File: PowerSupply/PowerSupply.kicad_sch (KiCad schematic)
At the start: 8 parts, among them J1 POWER, J2 CONTROL, J3 LASER, U0 AL8861Y-13

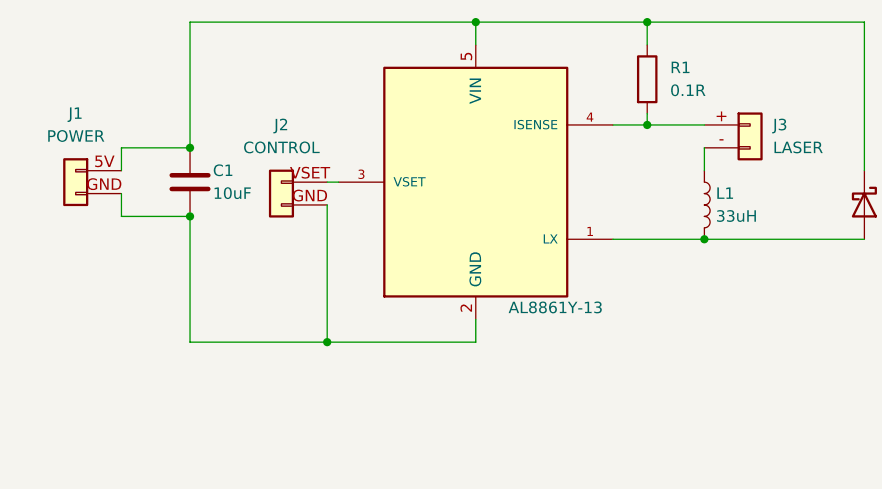
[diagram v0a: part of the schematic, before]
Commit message: update powersupply
edit resistor R1 (controling current) value, add pulldown on VSET, add descriptions
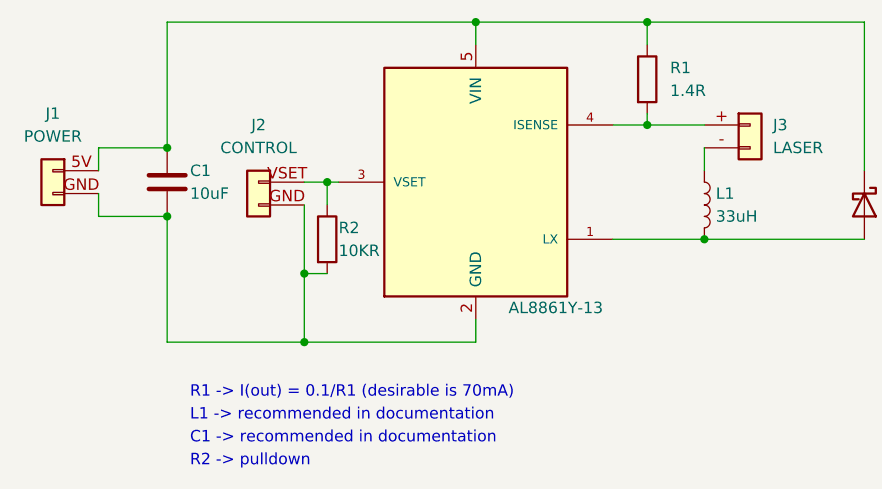
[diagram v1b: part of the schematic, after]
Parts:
- added R2: 10KR, symbol Device:R
- R1: value 0.1R -> 1.4R
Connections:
- net at C1.2, J1.GND, J2.GND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: now also R2.2
- net at J2.VSET, U0.3 (VSET): now also R2.1
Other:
- note added: "C1 -> recommended in documentation"
- note added: "L1 -> recommended in documentation"
- note added: "R1 -> I(out) = 0.1/R1 (desirable is 70mA)"
- note added: "R2 -> pulldown"
- moved on the sheet: C1, J1, J2
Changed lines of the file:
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@@
 (kicad_sch (version 20211123) (generator eeschema)
   (paper "A4")
-  (junction (at 110.49 90.17) (diameter 0) (color 0 0 0 0)
+  (junction (at 107.95 90.17) (diameter 0) (color 0 0 0 0)
   )
   (junction (at 161.29 76.2) (diameter 0) (color 0 0 0 0)
   )
-  (junction (at 125.73 111.76) (diameter 0) (color 0 0 0 0)
-  )
-  (junction (at 110.49 97.79) (diameter 0) (color 0 0 0 0)
+  (junction (at 107.95 97.79) (diameter 0) (color 0 0 0 0)
   )
   (junction (at 142.24 76.2) (diameter 0) (color 0 0 0 0)
   )
+  (junction (at 125.73 93.98) (diameter 0) (color 0 0 0 0)
+  )
   (junction (at 167.64 100.33) (diameter 0) (color 0 0 0 0)
   )
+  (junction (at 123.19 104.14) (diameter 0) (color 0 0 0 0)
+  )
+  (junction (at 123.19 111.76) (diameter 0) (color 0 0 0 0)
+  )
   (junction (at 161.29 87.63) (diameter 0) (color 0 0 0 0)
   )
-  (wire (pts (xy 102.87 92.71) (xy 102.87 90.17))
+  (wire (pts (xy 100.33 92.71) (xy 100.33 90.17))
     (stroke (width 0) (type default) (color 0 0 0 0))
   )
@@
     (stroke (width 0) (type default) (color 0 0 0 0))
   )
-  (wire (pts (xy 102.87 90.17) (xy 110.49 90.17))
-    (stroke (width 0) (type default) (color 0 0 0 0))
-  )
-  (wire (pts (xy 110.49 76.2) (xy 142.24 76.2))
+  (wire (pts (xy 123.19 104.14) (xy 125.73 104.14))
+    (stroke (width 0) (type default) (color 0 0 0 0))
+  )
+  (wire (pts (xy 100.33 90.17) (xy 107.95 90.17))
+    (stroke (width 0) (type default) (color 0 0 0 0))
+  )
+  (wire (pts (xy 107.95 76.2) (xy 142.24 76.2))
     (stroke (width 0) (type default) (color 0 0 0 0))
   )
@@
     (stroke (width 0) (type default) (color 0 0 0 0))
   )
-  (wire (pts (xy 110.49 97.79) (xy 110.49 111.76))
+  (wire (pts (xy 107.95 97.79) (xy 107.95 111.76))
     (stroke (width 0) (type default) (color 0 0 0 0))
   )
@@
     (stroke (width 0) (type default) (color 0 0 0 0))
   )
+  (wire (pts (xy 125.73 93.98) (xy 127 93.98))
+    (stroke (width 0) (type default) (color 0 0 0 0))
+  )
   (wire (pts (xy 185.42 76.2) (xy 161.29 76.2))
     (stroke (width 0) (type default) (color 0 0 0 0))
   )
-  (wire (pts (xy 125.73 111.76) (xy 142.24 111.76))
-    (stroke (width 0) (type default) (color 0 0 0 0))
-  )
   (wire (pts (xy 142.24 111.76) (xy 142.24 109.22))
     (stroke (width 0) (type default) (color 0 0 0 0))
   )
+  (wire (pts (xy 123.19 111.76) (xy 142.24 111.76))
+    (stroke (width 0) (type default) (color 0 0 0 0))
+  )
   (wire (pts (xy 142.24 76.2) (xy 161.29 76.2))
     (stroke (width 0) (type default) (color 0 0 0 0))
@@
     (stroke (width 0) (type default) (color 0 0 0 0))
   )
-  (wire (pts (xy 125.73 96.52) (xy 125.73 111.76))
-    (stroke (width 0) (type default) (color 0 0 0 0))
-  )
-  (wire (pts (xy 125.73 93.98) (xy 127 93.98))
-    (stroke (width 0) (type default) (color 0 0 0 0))
-  )
-  (wire (pts (xy 110.49 90.17) (xy 110.49 76.2))
-    (stroke (width 0) (type default) (color 0 0 0 0))
-  )
-  (wire (pts (xy 102.87 95.25) (xy 102.87 97.79))
+  (wire (pts (xy 123.19 96.52) (xy 123.19 104.14))
+    (stroke (width 0) (type default) (color 0 0 0 0))
+  )
+  (wire (pts (xy 123.19 104.14) (xy 123.19 111.76))
+    (stroke (width 0) (type default) (color 0 0 0 0))
+  )
+  (wire (pts (xy 123.19 93.98) (xy 125.73 93.98))
+    (stroke (width 0) (type default) (color 0 0 0 0))
+  )
+  (wire (pts (xy 107.95 90.17) (xy 107.95 76.2))
+    (stroke (width 0) (type default) (color 0 0 0 0))
+  )
+  (wire (pts (xy 125.73 93.98) (xy 125.73 96.52))
+    (stroke (width 0) (type default) (color 0 0 0 0))
+  )
+  (wire (pts (xy 100.33 95.25) (xy 100.33 97.79))
     (stroke (width 0) (type default) (color 0 0 0 0))
   )
@@
     (stroke (width 0) (type default) (color 0 0 0 0))
   )
-  (wire (pts (xy 110.49 111.76) (xy 125.73 111.76))
-    (stroke (width 0) (type default) (color 0 0 0 0))
-  )
-  (wire (pts (xy 102.87 97.79) (xy 110.49 97.79))
-    (stroke (width 0) (type default) (color 0 0 0 0))
+  (wire (pts (xy 107.95 111.76) (xy 123.19 111.76))
+    (stroke (width 0) (type default) (color 0 0 0 0))
+  )
+  (wire (pts (xy 100.33 97.79) (xy 107.95 97.79))
+    (stroke (width 0) (type default) (color 0 0 0 0))
+  )
+  (text "C1 -> recommended in documentation" (at 110.49 123.19 0)
+    (effects (font (size 1.27 1.27)) (justify left bottom))
+  )
+  (text "R2 -> pulldown" (at 110.49 125.73 0)
+    (effects (font (size 1.27 1.27)) (justify left bottom))
+  )
+  (text "R1 -> I(out) = 0.1/R1 (desirable is 70mA)" (at 110.49 118.11 0)
+    (effects (font (size 1.27 1.27)) (justify left bottom))
+  )
+  (text "L1 -> recommended in documentation\n" (at 110.49 120.65 0)
+    (effects (font (size 1.27 1.27)) (justify left bottom))
   )
   (symbol (lib_id "Connector_Generic:Conn_01x02") (at 172.72 87.63 0) (unit 1)
@@
       (effects (font (size 1.27 1.27)) (justify left))
     )
-    (property "Value" "0.1R" (id 1) (at 163.83 83.8199 0)
+    (property "Value" "1.4R" (id 1) (at 163.83 83.8199 0)
       (effects (font (size 1.27 1.27)) (justify left))
     )
@@
     (pin "5")
   )
+  (symbol (lib_id "Device:R") (at 125.73 100.33 0) (unit 1)
+    (in_bom yes) (on_board yes)
+    (property "Reference" "R2" (id 0) (at 127 99.06 0)
+      (effects (font (size 1.27 1.27)) (justify left))
+    )
+    (property "Value" "10KR" (id 1) (at 127 101.6 0)
+      (effects (font (size 1.27 1.27)) (justify left))
+    )
+    (property "Footprint" "" (id 2) (at 123.952 100.33 90)
+      (effects (font (size 1.27 1.27)) hide)
+    )
+    (property "Datasheet" "~" (id 3) (at 125.73 100.33 0)
+      (effects (font (size 1.27 1.27)) hide)
+    )
+    (pin "1")
+    (pin "2")
+  )
   (symbol (lib_id "Device:L") (at 167.64 96.52 0) (unit 1)
     (in_bom yes) (on_board yes) (fields_autoplaced)
@@
     (pin "2")
   )
-  (symbol (lib_name "Conn_01x02_1") (lib_id "Connector_Generic:Conn_01x02") (at 97.79 92.71 0) (mirror y) (unit 1)
-    (in_bom yes) (on_board yes) (fields_autoplaced)
-    (property "Reference" "J1" (id 0) (at 97.79 86.36 0))
-    (property "Value" "POWER" (id 1) (at 97.79 88.9 0))
-    (property "Footprint" "" (id 2) (at 97.79 92.71 0)
-      (effects (font (size 1.27 1.27)) hide)
-    )
-    (property "Datasheet" "~" (id 3) (at 97.79 92.71 0)
+  (symbol (lib_name "Conn_01x02_1") (lib_id "Connector_Generic:Conn_01x02") (at 95.25 92.71 0) (mirror y) (unit 1)
+    (in_bom yes) (on_board yes) (fields_autoplaced)
+    (property "Reference" "J1" (id 0) (at 95.25 86.36 0))
+    (property "Value" "POWER" (id 1) (at 95.25 88.9 0))
+    (property "Footprint" "" (id 2) (at 95.25 92.71 0)
+      (effects (font (size 1.27 1.27)) hide)
+    )
+    (property "Datasheet" "~" (id 3) (at 95.25 92.71 0)
       (effects (font (size 1.27 1.27)) hide)
     )
@@
     (pin "GND")
   )
-  (symbol (lib_name "Conn_01x02_2") (lib_id "Connector_Generic:Conn_01x02") (at 120.65 93.98 0) (mirror y) (unit 1)
-    (in_bom yes) (on_board yes) (fields_autoplaced)
-    (property "Reference" "J2" (id 0) (at 120.65 87.63 0))
-    (property "Value" "CONTROL" (id 1) (at 120.65 90.17 0))
-    (property "Footprint" "" (id 2) (at 120.65 93.98 0)
-      (effects (font (size 1.27 1.27)) hide)
-    )
-    (property "Datasheet" "~" (id 3) (at 120.65 93.98 0)
-      (effects (font (size 1.27 1.27)) hide)
-    )
+  (symbol (lib_name "Conn_01x02_2") (lib_id "Connector_Generic:Conn_01x02") (at 118.11 93.98 0) (mirror y) (unit 1)
+    (in_bom yes) (on_board yes) (fields_autoplaced)
+    (property "Reference" "J2" (id 0) (at 118.11 87.63 0))
+    (property "Value" "CONTROL" (id 1) (at 118.11 90.17 0))
+    (property "Footprint" "" (id 2) (at 118.11 93.98 0)
+      (effects (font (size 1.27 1.27)) hide)
+    )
+    (property "Datasheet" "~" (id 3) (at 118.11 93.98 0)
+      (effects (font (size 1.27 1.27)) hide)
+    )
+    (pin "GND")
     (pin "VSET")
-    (pin "GND")
-  )
-  (symbol (lib_id "Device:C") (at 110.49 93.98 0) (unit 1)
-    (in_bom yes) (on_board yes)
-    (property "Reference" "C1" (id 0) (at 113.03 92.71 0)
-      (effects (font (size 1.27 1.27)) (justify left))
-    )
-    (property "Value" "10uF" (id 1) (at 113.03 95.25 0)
-      (effects (font (size 1.27 1.27)) (justify left))
-    )
-    (property "Footprint" "" (id 2) (at 111.4552 97.79 0)
-      (effects (font (size 1.27 1.27)) hide)
-    )
-    (property "Datasheet" "~" (id 3) (at 110.49 93.98 0)
+  )
+  (symbol (lib_id "Device:C") (at 107.95 93.98 0) (unit 1)
+    (in_bom yes) (on_board yes)
+    (property "Reference" "C1" (id 0) (at 110.49 92.71 0)
+      (effects (font (size 1.27 1.27)) (justify left))
+    )
+    (property "Value" "10uF" (id 1) (at 110.49 95.25 0)
+      (effects (font (size 1.27 1.27)) (justify left))
+    )
+    (property "Footprint" "" (id 2) (at 108.9152 97.79 0)
+      (effects (font (size 1.27 1.27)) hide)
+    )
+    (property "Datasheet" "~" (id 3) (at 107.95 93.98 0)
       (effects (font (size 1.27 1.27)) hide)
     )
@@
     )
     (path "/215b2e5e-51c1-496c-bbe4-577e5f55ea8b"
-      (reference "R1") (unit 1) (value "0.1R") (footprint "")
+      (reference "R1") (unit 1) (value "1.4R") (footprint "")
+    )
+    (path "/5026d3f3-4320-4298-9a32-8d0f6f66cc7d"
+      (reference "R2") (unit 1) (value "10KR") (footprint "")
     )
     (path "/31ddefd3-1a8e-42d5-a5b9-a7a71a2b2753"

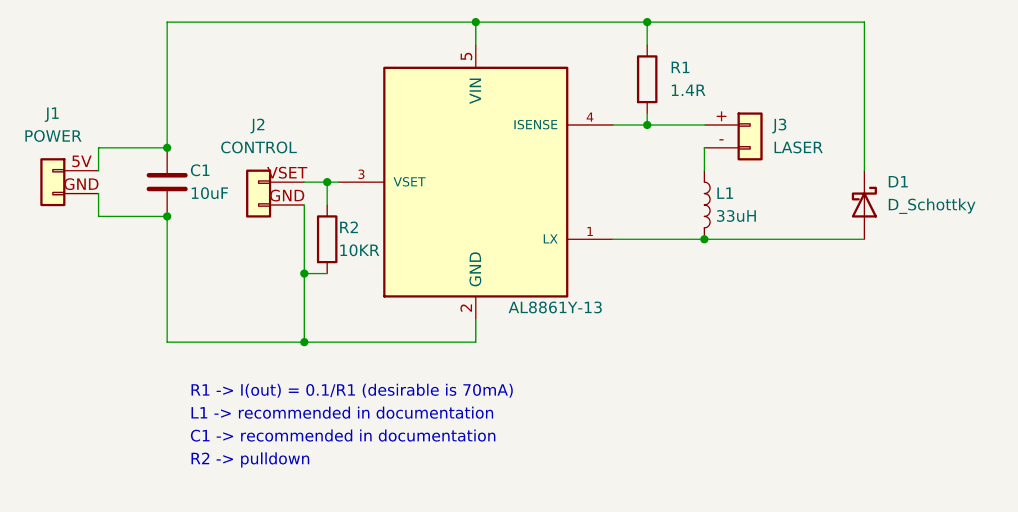
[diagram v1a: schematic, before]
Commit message: edit footprints
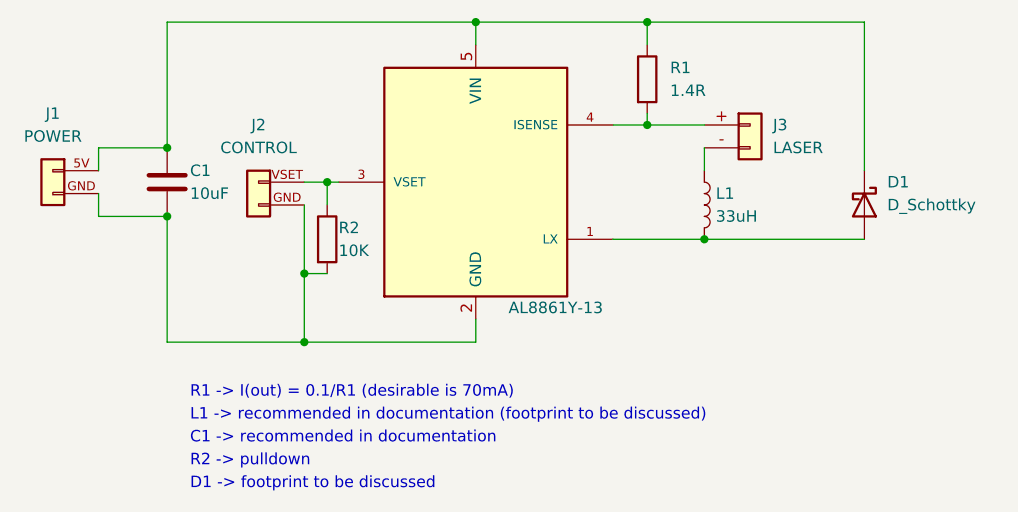
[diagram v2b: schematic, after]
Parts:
- C1: footprint (none) -> Capacitor_SMD:C_1206_3216Metric_Pad1.33x1.80mm_HandSolder
- D1: footprint (none) -> Diode_SMD:D_1206_3216Metric_Pad1.42x1.75mm_HandSolder
- J1, J2, J3: footprint (none) -> Connector_PinHeader_2.54mm:PinHeader_1x02_P2.54mm_Vertical
- L1: footprint (none) -> Inductor_SMD:L_1206_3216Metric_Pad1.42x1.75mm_HandSolder
- R1: footprint (none) -> Resistor_SMD:R_1206_3216Metric_Pad1.30x1.75mm_HandSolder
- R2: value 10KR -> 10K; footprint (none) -> Resistor_SMD:R_1206_3216Metric_Pad1.30x1.75mm_HandSolder
- U0: footprint CONV_AL8861Y-13 -> Package_TO_SOT_SMD:SOT-89-5
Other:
- note added: "D1 -> footprint to be discussed"
- note added: "L1 -> recommended in documentation (footprint to be discussed)"
- note removed: "L1 -> recommended in documentation"
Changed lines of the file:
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@@
+    (effects (font (size 1.27 1.27)) (justify left bottom))
+  )
+  (text "D1 -> footprint to be discussed" (at 110.49 128.27 0)
     (effects (font (size 1.27 1.27)) (justify left bottom))
   )
@@
     (effects (font (size 1.27 1.27)) (justify left bottom))
   )
-  (text "L1 -> recommended in documentation\n" (at 110.49 120.65 0)
+  (text "L1 -> recommended in documentation (footprint to be discussed)\n"
+    (at 110.49 120.65 0)
     (effects (font (size 1.27 1.27)) (justify left bottom))
   )
@@
       (effects (font (size 1.27 1.27)) (justify left))
     )
-    (property "Footprint" "" (id 2) (at 172.72 87.63 0)
+    (property "Footprint" "Connector_PinHeader_2.54mm:PinHeader_1x02_P2.54mm_Vertical" (id 2) (at 172.72 87.63 0)
       (effects (font (size 1.27 1.27)) hide)
     )
@@
       (effects (font (size 1.27 1.27)) (justify left))
     )
-    (property "Footprint" "" (id 2) (at 159.512 82.55 90)
+    (property "Footprint" "Resistor_SMD:R_1206_3216Metric_Pad1.30x1.75mm_HandSolder" (id 2) (at 159.512 82.55 90)
       (effects (font (size 1.27 1.27)) hide)
     )
@@
     )
     (property "Value" "AL8861Y-13" (id 1) (at 151.13 107.95 0))
-    (property "Footprint" "CONV_AL8861Y-13" (id 2) (at 157.48 82.55 0)
+    (property "Footprint" "Package_TO_SOT_SMD:SOT-89-5" (id 2) (at 157.48 82.55 0)
       (effects (font (size 1.27 1.27)) (justify left bottom) hide)
     )
@@
       (effects (font (size 1.27 1.27)) (justify left))
     )
-    (property "Value" "10KR" (id 1) (at 127 101.6 0)
-      (effects (font (size 1.27 1.27)) (justify left))
-    )
-    (property "Footprint" "" (id 2) (at 123.952 100.33 90)
+    (property "Value" "10K" (id 1) (at 127 101.6 0)
+      (effects (font (size 1.27 1.27)) (justify left))
+    )
+    (property "Footprint" "Resistor_SMD:R_1206_3216Metric_Pad1.30x1.75mm_HandSolder" (id 2) (at 123.952 100.33 90)
       (effects (font (size 1.27 1.27)) hide)
     )
@@
       (effects (font (size 1.27 1.27)) (justify left))
     )
-    (property "Footprint" "" (id 2) (at 167.64 96.52 0)
+    (property "Footprint" "Inductor_SMD:L_1206_3216Metric_Pad1.42x1.75mm_HandSolder" (id 2) (at 167.64 96.52 0)
       (effects (font (size 1.27 1.27)) hide)
     )
@@
     (property "Reference" "J1" (id 0) (at 95.25 86.36 0))
     (property "Value" "POWER" (id 1) (at 95.25 88.9 0))
-    (property "Footprint" "" (id 2) (at 95.25 92.71 0)
+    (property "Footprint" "Connector_PinHeader_2.54mm:PinHeader_1x02_P2.54mm_Vertical" (id 2) (at 95.25 88.9 0)
       (effects (font (size 1.27 1.27)) hide)
     )
@@
     (property "Reference" "J2" (id 0) (at 118.11 87.63 0))
     (property "Value" "CONTROL" (id 1) (at 118.11 90.17 0))
-    (property "Footprint" "" (id 2) (at 118.11 93.98 0)
+    (property "Footprint" "Connector_PinHeader_2.54mm:PinHeader_1x02_P2.54mm_Vertical" (id 2) (at 118.11 93.98 0)
       (effects (font (size 1.27 1.27)) hide)
     )
@@
       (effects (font (size 1.27 1.27)) (justify left))
     )
-    (property "Footprint" "" (id 2) (at 108.9152 97.79 0)
+    (property "Footprint" "Capacitor_SMD:C_1206_3216Metric_Pad1.33x1.80mm_HandSolder" (id 2) (at 108.9152 97.79 0)
       (effects (font (size 1.27 1.27)) hide)
     )
@@
       (effects (font (size 1.27 1.27)) (justify left))
     )
-    (property "Footprint" "" (id 2) (at 185.42 96.52 0)
+    (property "Footprint" "Diode_SMD:D_1206_3216Metric_Pad1.42x1.75mm_HandSolder" (id 2) (at 185.42 96.52 0)
       (effects (font (size 1.27 1.27)) hide)
     )
@@
   (symbol_instances
     (path "/e6097f1c-f948-4071-ba94-c5c243a0ace3"
-      (reference "C1") (unit 1) (value "10uF") (footprint "")
+      (reference "C1") (unit 1) (value "10uF") (footprint "Capacitor_SMD:C_1206_3216Metric_Pad1.33x1.80mm_HandSolder")
     )
     (path "/f8b9e1e3-f546-4bb6-b947-aecd649c1451"
-      (reference "D1") (unit 1) (value "D_Schottky") (footprint "")
+      (reference "D1") (unit 1) (value "D_Schottky") (footprint "Diode_SMD:D_1206_3216Metric_Pad1.42x1.75mm_HandSolder")
     )
     (path "/772a2ded-0d86-487f-aa29-160aff6a24b0"
-      (reference "J1") (unit 1) (value "POWER") (footprint "")
+      (reference "J1") (unit 1) (value "POWER") (footprint "Connector_PinHeader_2.54mm:PinHeader_1x02_P2.54mm_Vertical")
     )
     (path "/b78029a9-e0d1-49f5-bb8a-4b0a6160196f"
-      (reference "J2") (unit 1) (value "CONTROL") (footprint "")
+      (reference "J2") (unit 1) (value "CONTROL") (footprint "Connector_PinHeader_2.54mm:PinHeader_1x02_P2.54mm_Vertical")
     )
     (path "/1f624ff1-b4e4-4cd6-9b31-c6d56c779d5c"
-      (reference "J3") (unit 1) (value "LASER") (footprint "")
+      (reference "J3") (unit 1) (value "LASER") (footprint "Connector_PinHeader_2.54mm:PinHeader_1x02_P2.54mm_Vertical")
     )
     (path "/6d2c135f-c5da-4eb0-aeed-fa50fc1aef8c"
-      (reference "L1") (unit 1) (value "33uH") (footprint "")
+      (reference "L1") (unit 1) (value "33uH") (footprint "Inductor_SMD:L_1206_3216Metric_Pad1.42x1.75mm_HandSolder")
     )
     (path "/215b2e5e-51c1-496c-bbe4-577e5f55ea8b"
-      (reference "R1") (unit 1) (value "1.4R") (footprint "")
+      (reference "R1") (unit 1) (value "1.4R") (footprint "Resistor_SMD:R_1206_3216Metric_Pad1.30x1.75mm_HandSolder")
     )
     (path "/5026d3f3-4320-4298-9a32-8d0f6f66cc7d"
-      (reference "R2") (unit 1) (value "10KR") (footprint "")
+      (reference "R2") (unit 1) (value "10K") (footprint "Resistor_SMD:R_1206_3216Metric_Pad1.30x1.75mm_HandSolder")
     )
     (path "/31ddefd3-1a8e-42d5-a5b9-a7a71a2b2753"
-      (reference "U0") (unit 1) (value "AL8861Y-13") (footprint "CONV_AL8861Y-13")
-    )
-  )
+      (reference "U0") (unit 1) (value "AL8861Y-13") (footprint "Package_TO_SOT_SMD:SOT-89-5")
+    )
+  )
